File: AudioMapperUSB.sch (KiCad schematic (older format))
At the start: 154 parts, among them J1 USB_B, J10 Conn_01x01, J11 Conn_01x01, J12 Jack-DC, J13 Conn_01x02, J14 Conn_01x02, J16 Audio-Jack-2, J17 Audio-Jack-2, J18 Audio-Jack-2, J19 Audio-Jack-2, J2 Audio-Jack-2, J20 Audio-Jack-2, J21 Audio-Jack-2, J3 Conn_01x02, J4 Audio-Jack-2, J5 Conn_01x02, J6 Conn_01x02, J7 Conn_01x02, J8 Conn_01x01, J9 Conn_01x01, Q1 SS8550, U1 AMS1117-3.3, U2 PCM2900, U3 OPA2170, U4 OPA2170, U5 OPA2170, U6 OPA2170, U7 KA78M05_TO252, U8 74HC04, Y1 12 MHz

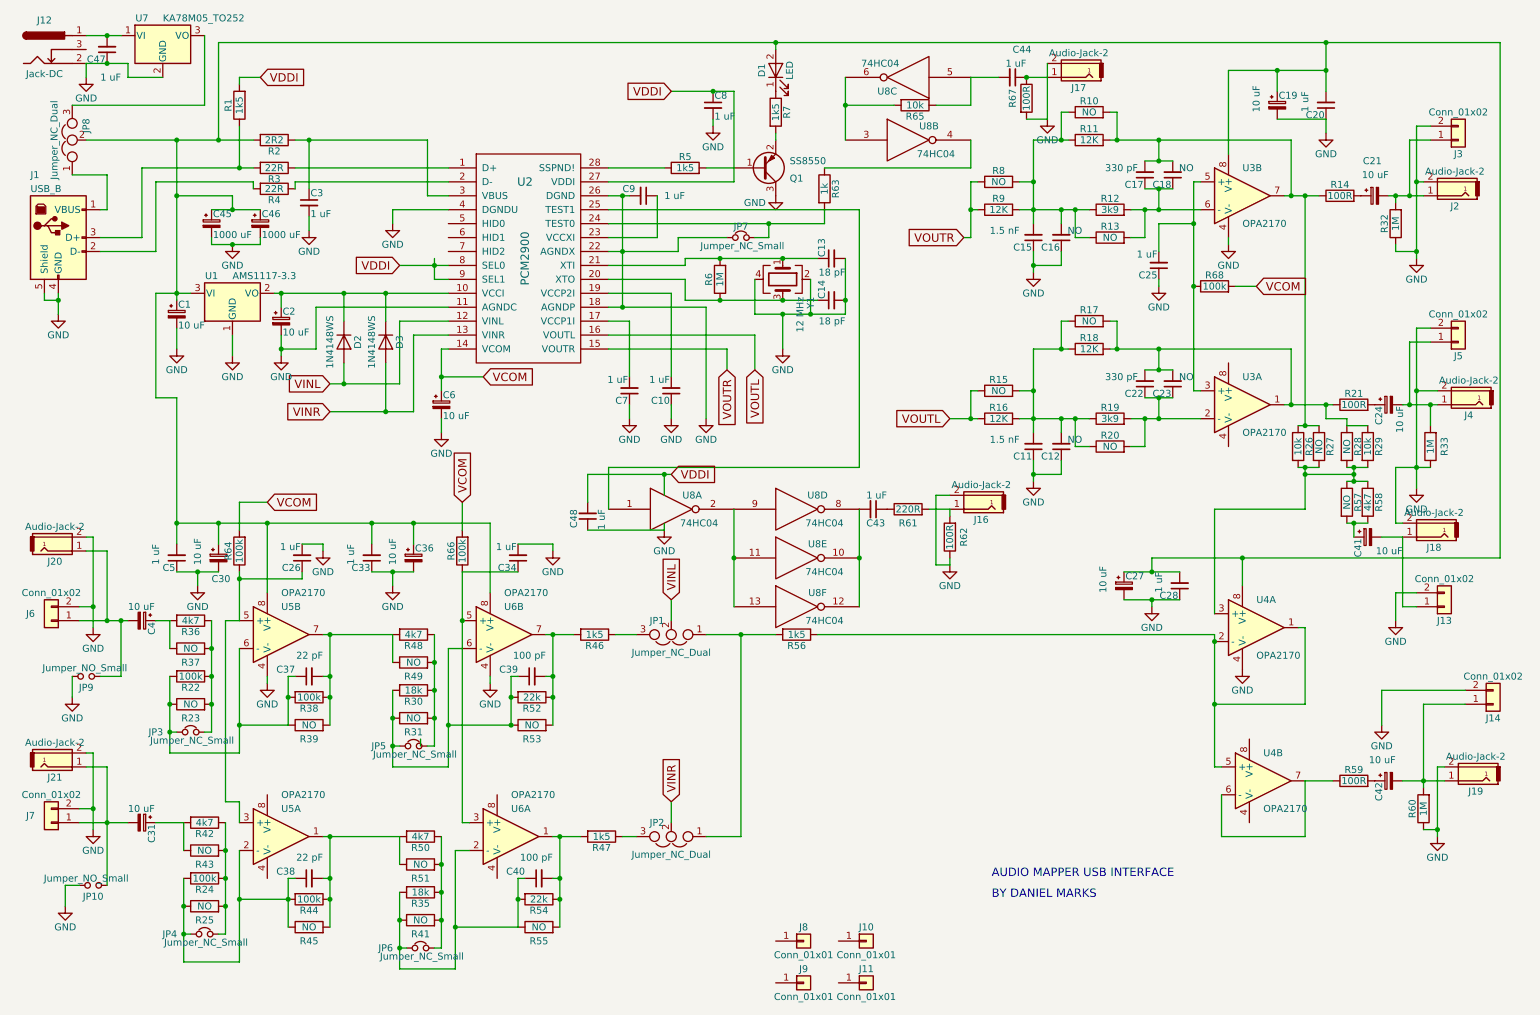
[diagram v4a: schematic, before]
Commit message: Added balanced outputs
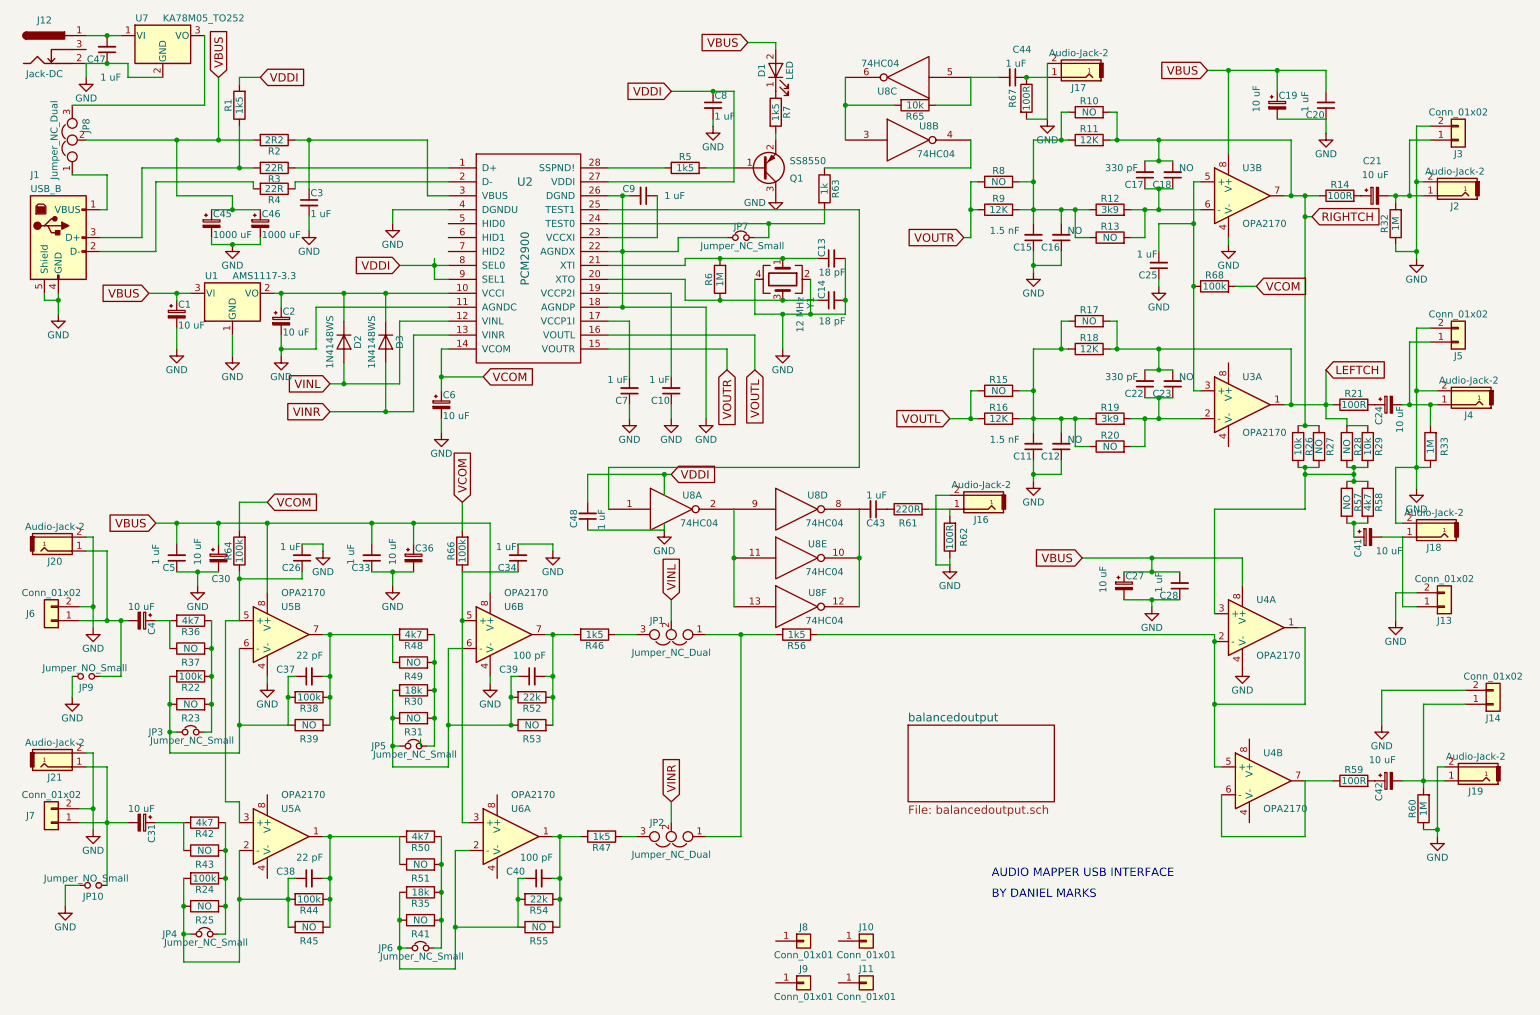
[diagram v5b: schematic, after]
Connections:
- net VBUS: now reaches C1.1, C19.1, C20.2, C27.1, C28.2, C30.1, C33.2, C36.1, C45.1, C46.1, C5.2, D1.2 (A), JP8.2, R2.2, U1.3 (VI), U3.8 (V+), U4.8 (V+), U5.8 (V+), U6.8 (V+)
- net LEFTCH: now reaches C22.2, C23.2, R17.2, R18.2, R21.1, R28.1, R29.1, U3.1
- net RIGHTCH: now reaches C17.2, C18.2, R10.2, R11.2, R14.1, R26.1, R27.1, U3.7
